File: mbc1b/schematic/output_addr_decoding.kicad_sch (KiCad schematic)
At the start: 21 parts

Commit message: Typo
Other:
- title: MBC1B - Addess Decoding (outputs) -> MBC1B - Address Decoding (outputs)
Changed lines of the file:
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@@
   (paper "A4")
   (title_block
-    (title "MBC1B - Addess Decoding (outputs)")
+    (title "MBC1B - Address Decoding (outputs)")
     (date "2022-03-13")
     (rev "A")

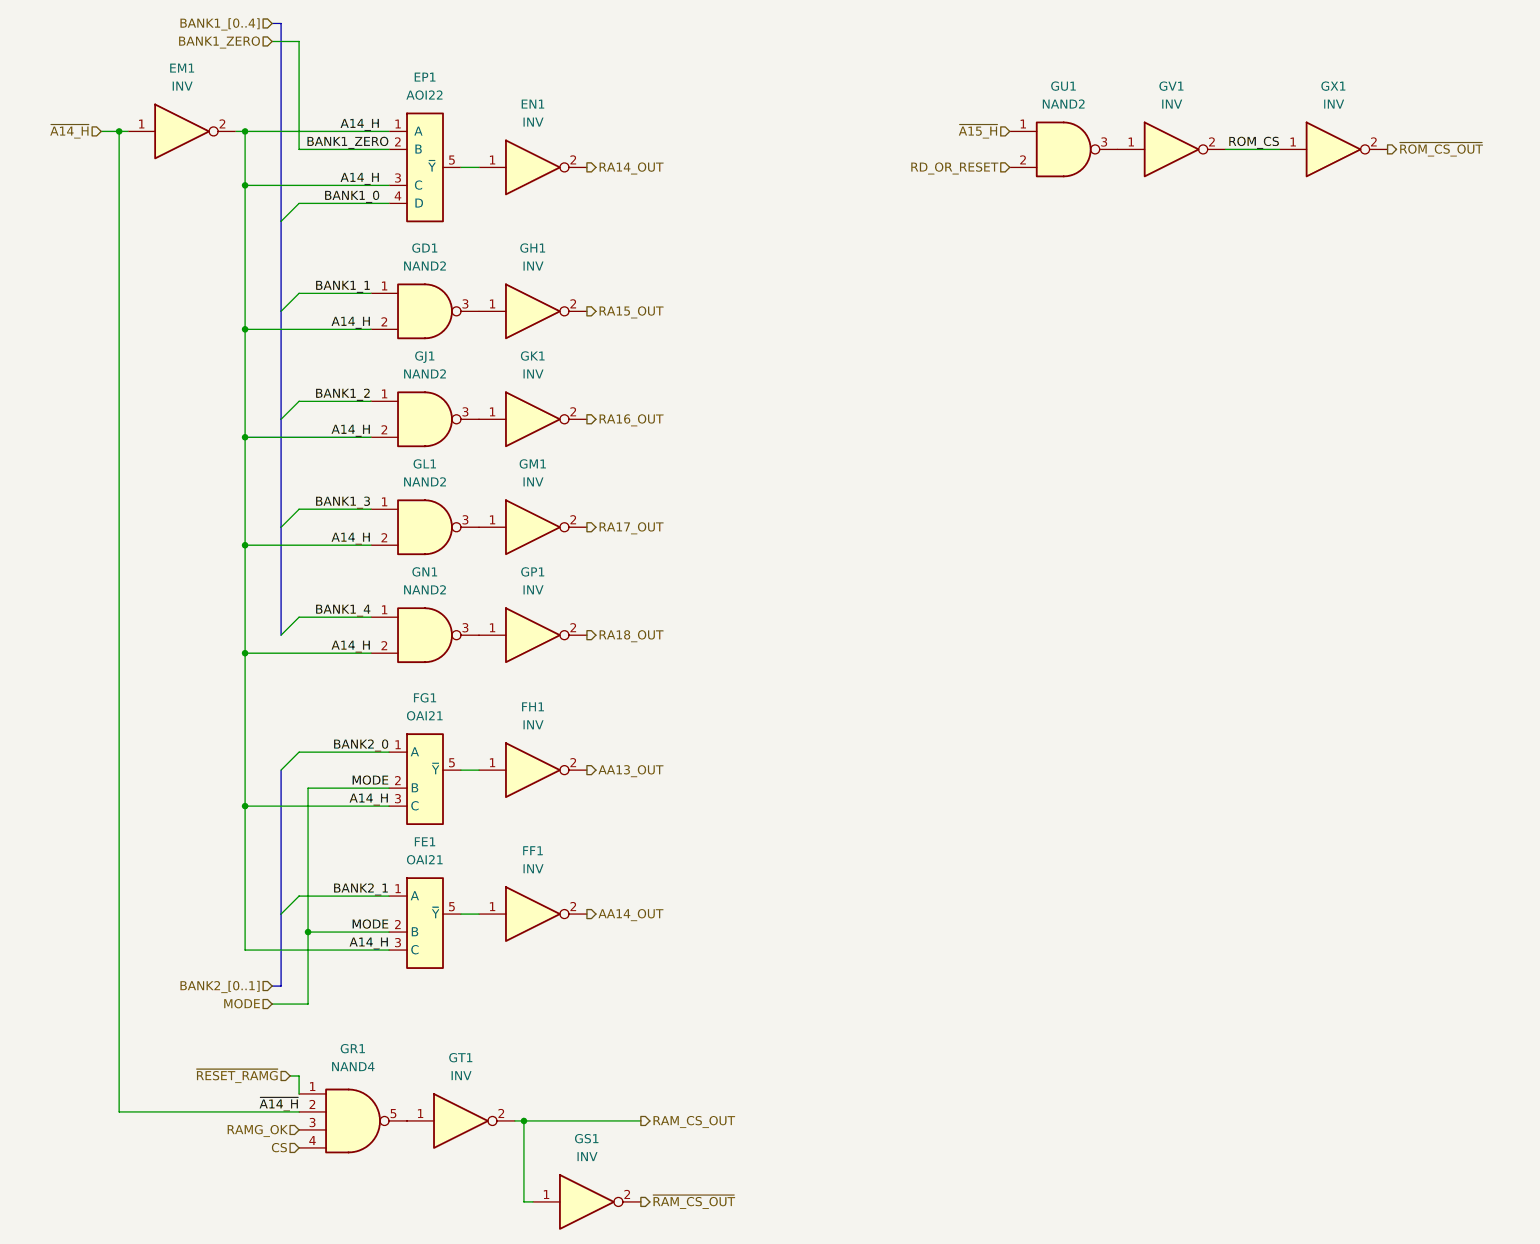
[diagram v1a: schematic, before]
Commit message: Update MBC1B schematic with latest kingfish compatibility
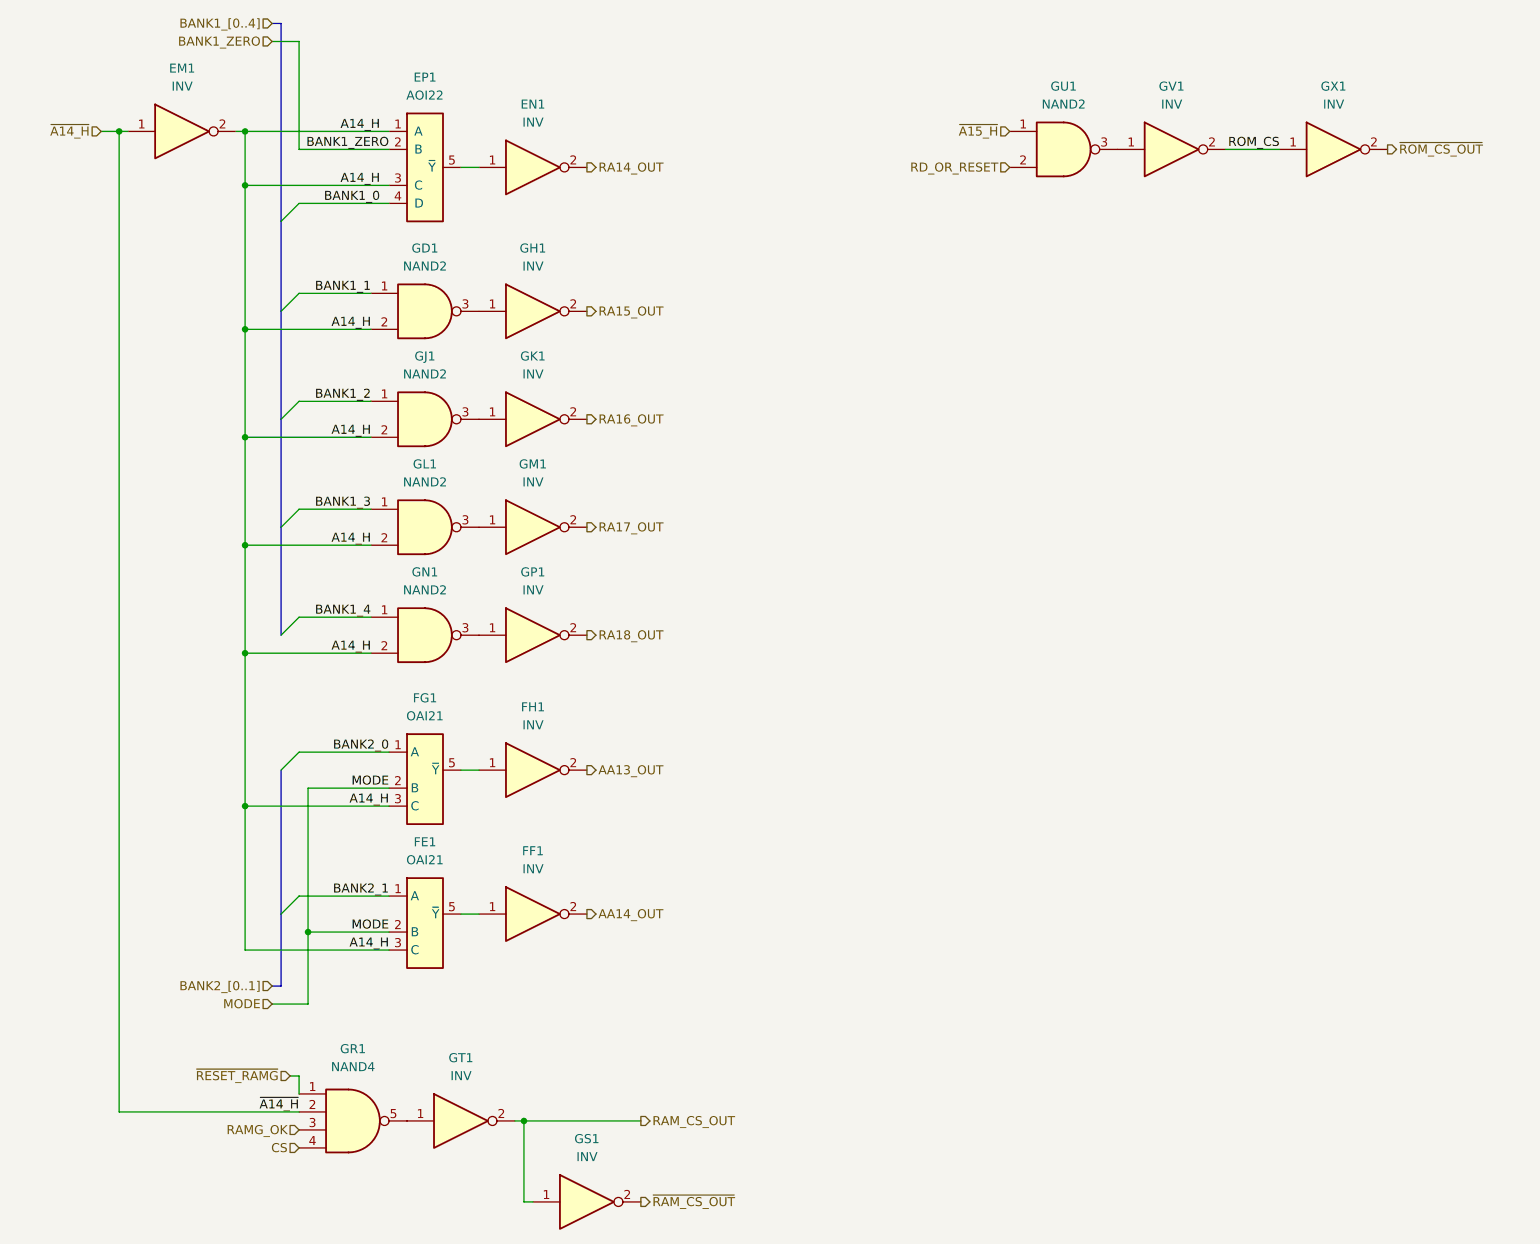
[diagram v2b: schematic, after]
